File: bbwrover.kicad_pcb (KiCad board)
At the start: 2 copper layers, 60 x 49.1 mm, 20 parts, among them J1 UART2, J10 Power Conn., J2 Conn, J3 Conn, J4 Conn, J5 Conn, J6 Conn, J7 Conn, J8 Conn, J9 UART1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

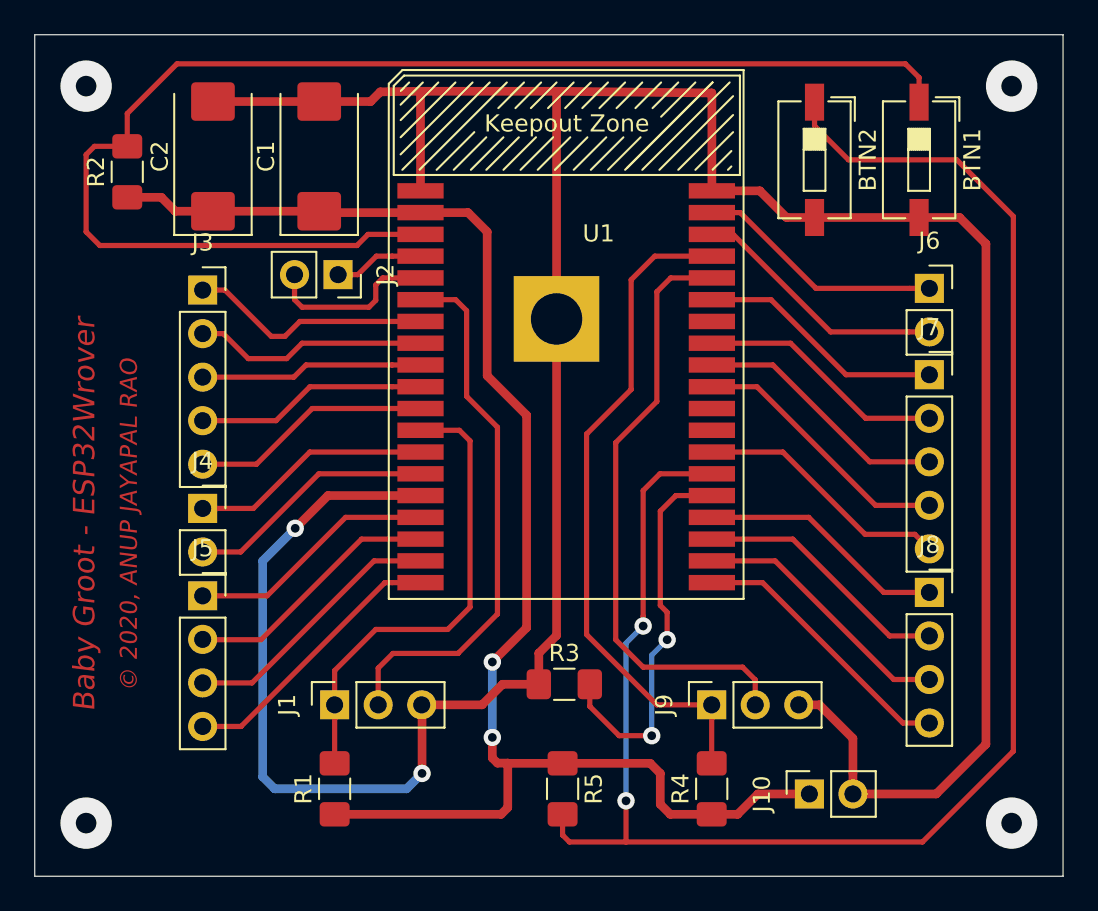
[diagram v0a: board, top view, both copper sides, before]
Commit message: Added filled zone  for the PCB
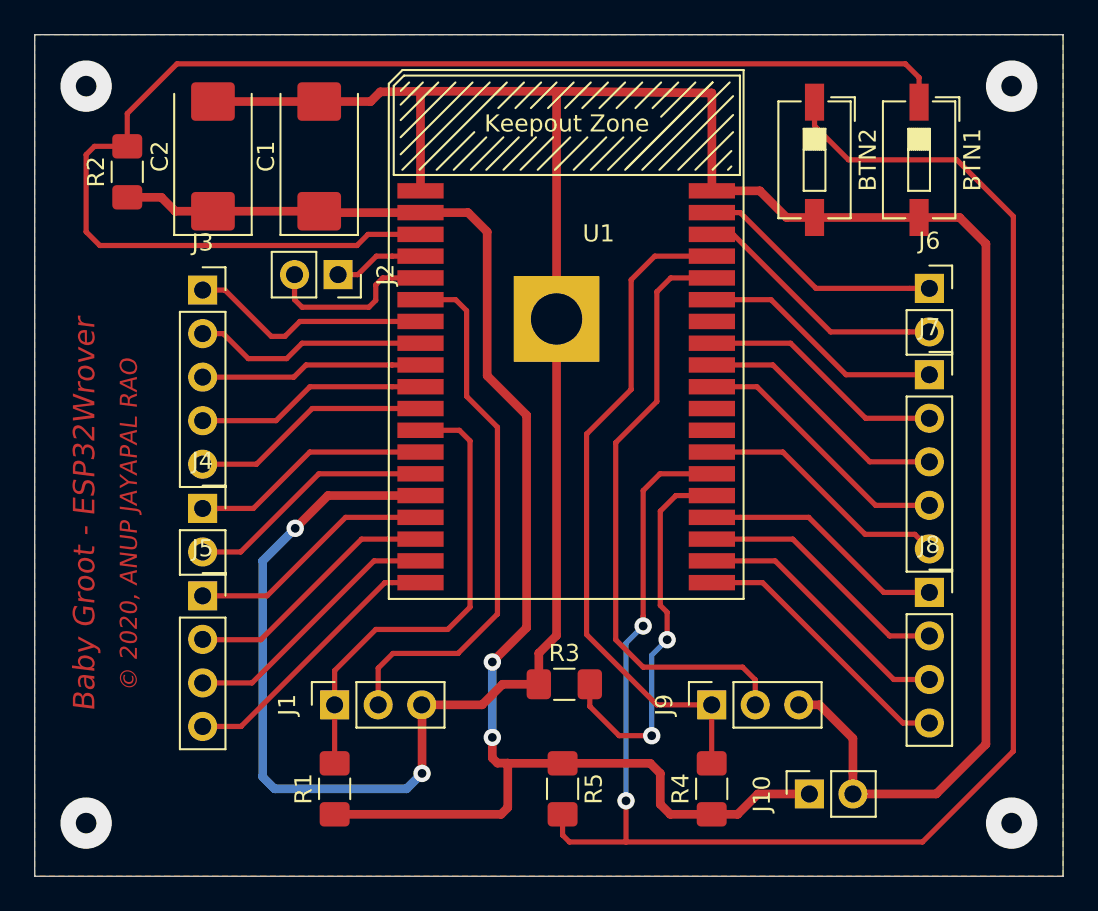
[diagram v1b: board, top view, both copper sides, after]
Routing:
- added copper zone on F.Cu, net GND
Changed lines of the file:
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@@
     (user_trace_width 0.508)
     (trace_clearance 0.2)
-    (zone_clearance 0.508)
+    (zone_clearance 0.6)
     (zone_45_only no)
     (trace_min 0.2)
@@
   (segment (start 139.510001 104.890001) (end 137.409999 104.890001) (width 0.3048) (layer F.Cu) (net 33))
   (segment (start 137.409999 104.890001) (end 136.5 105.8) (width 0.3048) (layer F.Cu) (net 33))
+  (zone (net 2) (net_name GND) (layer F.Cu) (hatch edge 0.508)
+    (connect_pads (clearance 0.6))
+    (min_thickness 0.254)
+    (fill yes (arc_segments 32) (thermal_gap 0.6) (thermal_bridge_width 0.6) (smoothing chamfer))
+    (polygon
+      (pts
+        (xy 160 127.1) (xy 100 127.1) (xy 100 78) (xy 160 78)
+      )
+    )
+  )
 )
